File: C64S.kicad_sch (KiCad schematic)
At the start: 3 parts, among them J1 DATASETTE PORT, J2 DB25_Plug, J3 Barrel_Jack_Switch

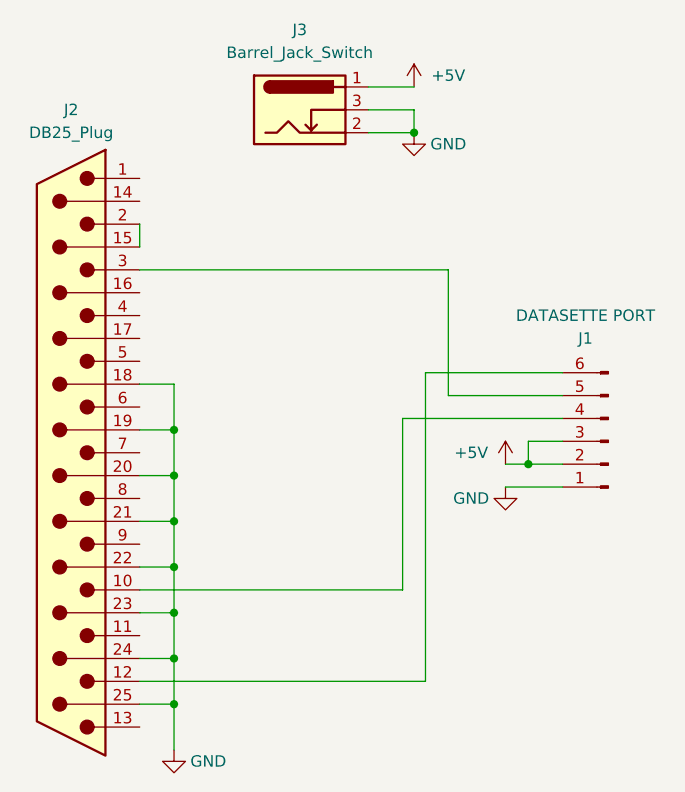
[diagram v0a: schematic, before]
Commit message: Add LCSC part no's, website address and update schematic
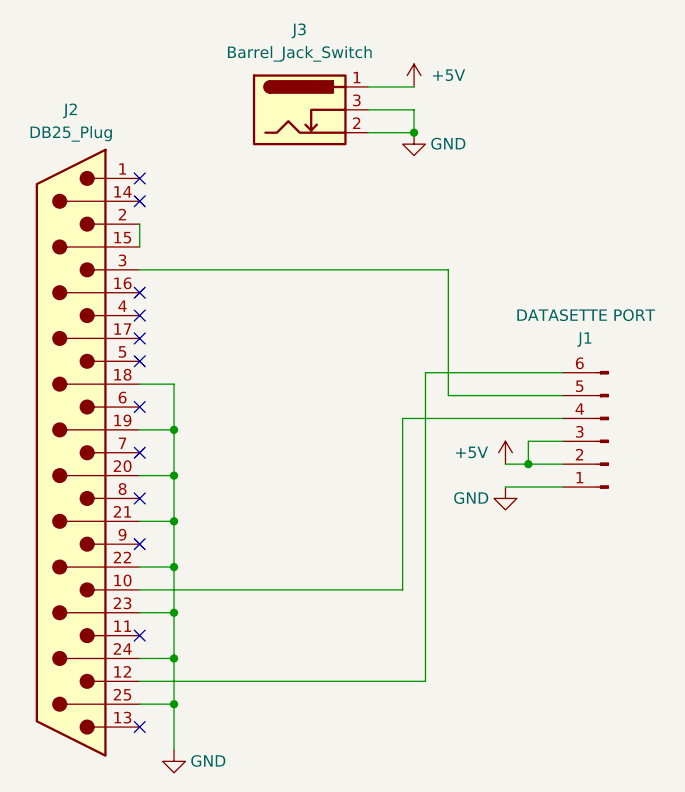
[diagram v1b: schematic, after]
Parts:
- J1: now left out of the parts list
- J2: LCSC (none) -> C75745
- J3: LCSC (none) -> C16214
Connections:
- no-connect marks 0 -> 12
